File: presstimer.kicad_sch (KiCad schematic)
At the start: 38 parts, among them J1 Screw_Terminal_01x02, J3 Connector, USB-TYPE-C-16P, Q1 NPN, Q2 NPN, SW1 SW_Push, SW2 SW_Push, U1 AP7361C-33ER, U2 ESP32-S3-WROOM-1

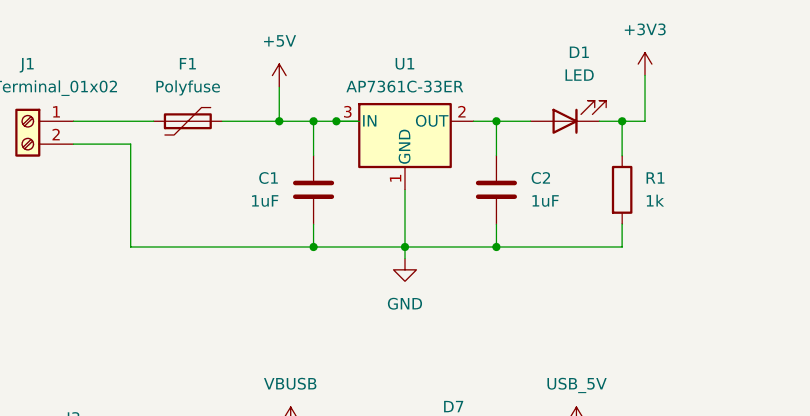
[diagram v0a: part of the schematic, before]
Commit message: footprints added, pcb started
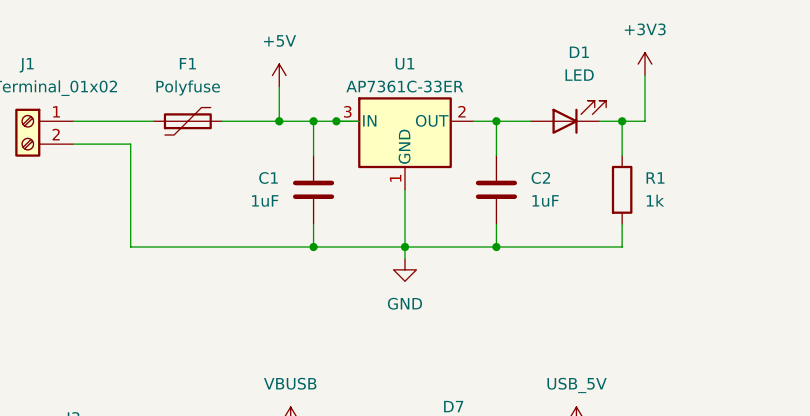
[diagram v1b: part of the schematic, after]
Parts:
- J1: footprint (none) -> markus:DG305-5.0-02P-12-00A(H)
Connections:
- new net OUT: U1.4 (OUT)
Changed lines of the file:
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@@
 			)
 		)
-		(property "Footprint" ""
+		(property "Footprint" "markus:DG305-5.0-02P-12-00A(H)"
 			(at 26.67 26.67 0)
 			(hide yes)
@@
 		(pin "1"
 		)
+		(pin "4"
+		)
 		(instances

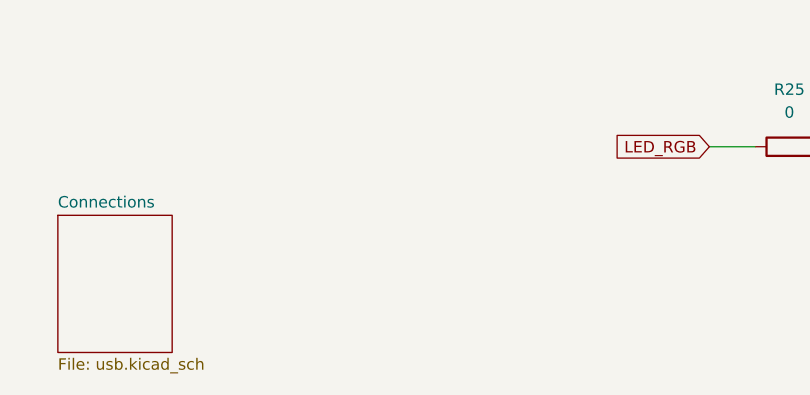
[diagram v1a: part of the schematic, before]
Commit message: usb-uart added to schematic
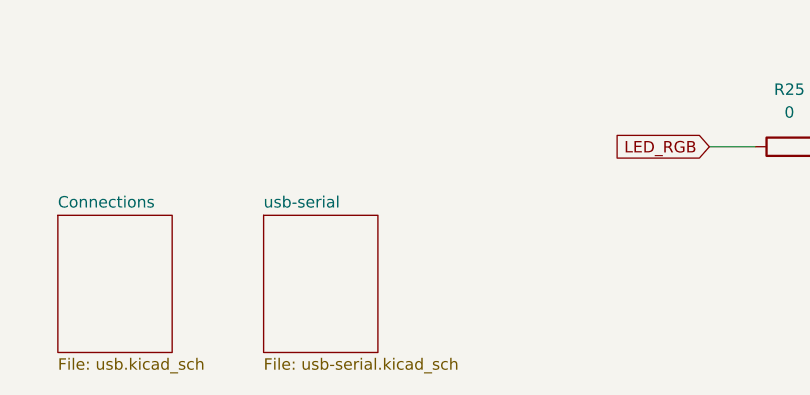
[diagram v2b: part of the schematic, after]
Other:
- added sheet usb-serial (usb-serial.kicad_sch)
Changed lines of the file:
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@@
+	)
+	(sheet
+		(at 66.04 177.8)
+		(size 12.7 15.24)
+		(exclude_from_sim no)
+		(in_bom yes)
+		(on_board yes)
+		(dnp no)
+		(fields_autoplaced yes)
+		(stroke
+			(width 0.1524)
+			(type solid)
+		)
+		(fill
+			(color 0 0 0 0)
+		)
+		(property "Sheetname" "usb-serial"
+			(at 66.04 177.0884 0)
+			(show_name no)
+			(do_not_autoplace no)
+			(effects
+				(font
+					(size 1.27 1.27)
+				)
+				(justify left bottom)
+			)
+		)
+		(property "Sheetfile" "usb-serial.kicad_sch"
+			(at 66.04 193.6246 0)
+			(show_name no)
+			(do_not_autoplace no)
+			(effects
+				(font
+					(size 1.27 1.27)
+				)
+				(justify left top)
+			)
+		)
+		(instances
+			(project "presstimer"
+				(path "/63494a82-20b5-470b-977d-6a82bfa70174"
+					(page "3")
+				)
+			)
+		)
 	)
 	(sheet

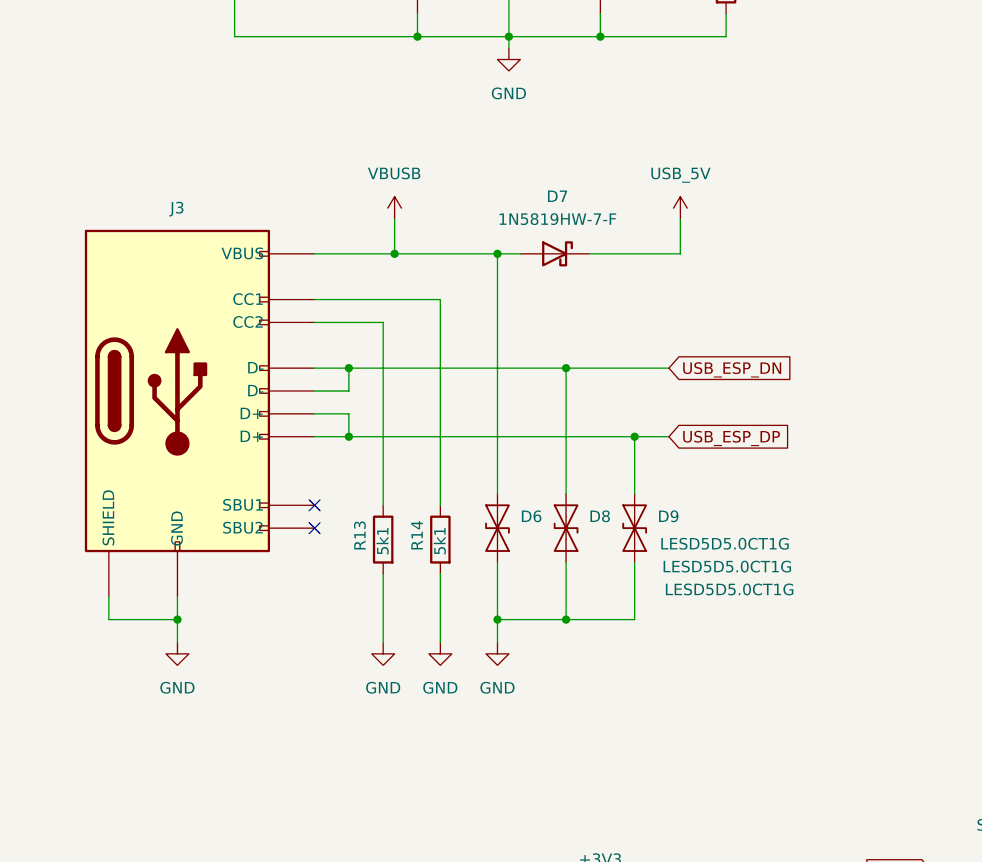
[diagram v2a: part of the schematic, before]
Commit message: added usb-serial programmer and footprints
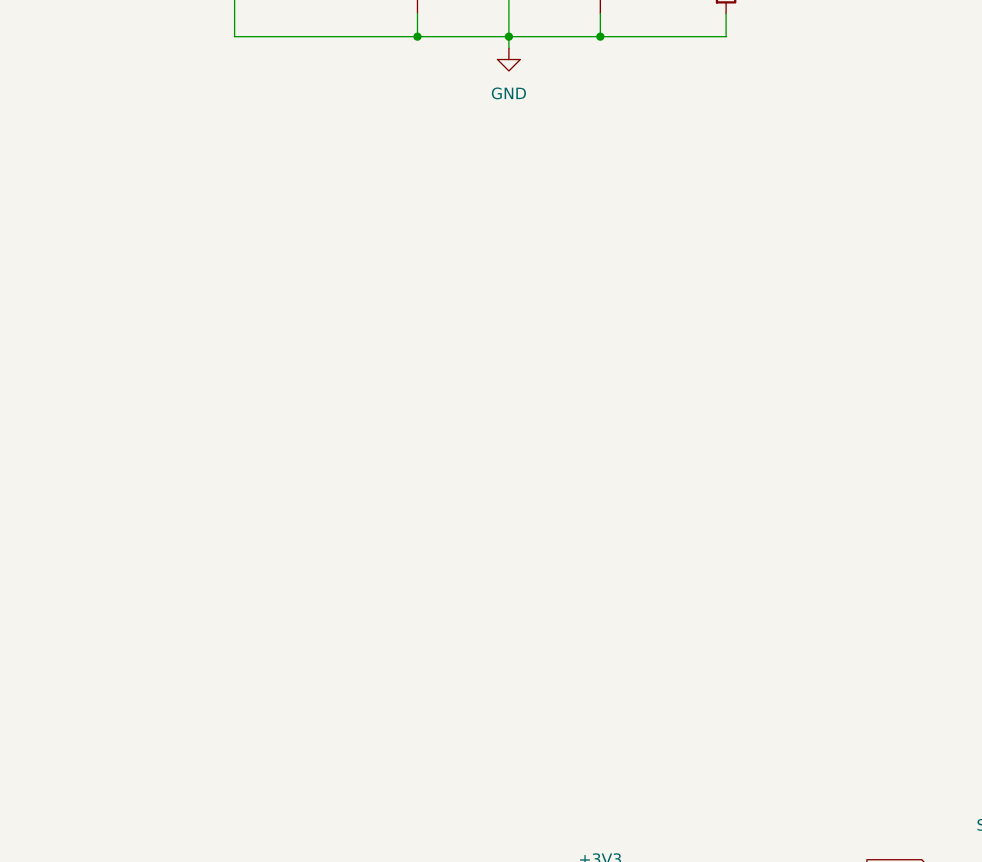
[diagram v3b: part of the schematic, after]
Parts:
- removed D6, D8, D9: LESD5D5.0CT1G, PCM_JLCPCB:D_SOD-523, symbol Diode:ESD131-B1-W0201
- removed D7: 1N5819HW-7-F, Diode_SMD:D_SOD-123, symbol markus:1N5819HW-7-F
- removed J3: Connector, USB-TYPE-C-16P, PCM_JLCPCB:TYPE-C-SMD_HX-TYPE-C-16PIN, symbol PCM_JLCPCB-Extended:Connector, USB-TYPE-C-16P
- removed R13, R14: 5k1, PCM_JLCPCB:R_0603, symbol Device:R
- R25: footprint PCM_JLCPCB:R_1206 -> PCM_JLCPCB:R_0805
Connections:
- no-connect marks 9 -> 7
